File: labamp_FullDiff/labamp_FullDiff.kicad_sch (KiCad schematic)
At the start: 30 parts, among them J1 Conn_02x06_Odd_Even, J2 Conn_02x06_Odd_Even, J3 Conn_01x03, U3 THS4521ID

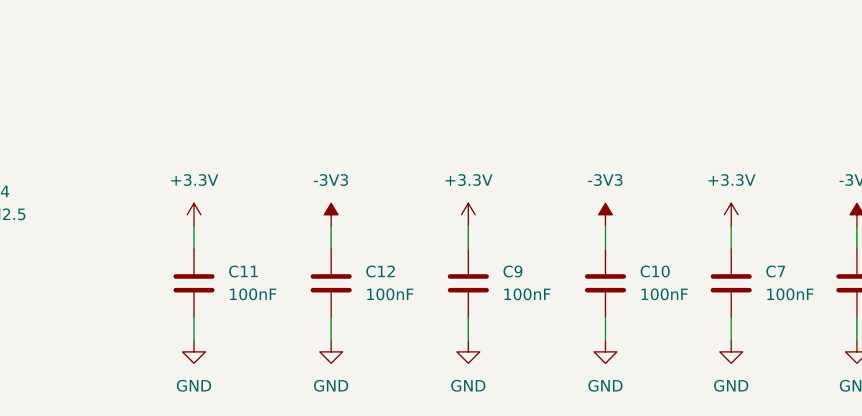
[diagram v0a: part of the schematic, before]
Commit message: PCB layout od Diff ampl started
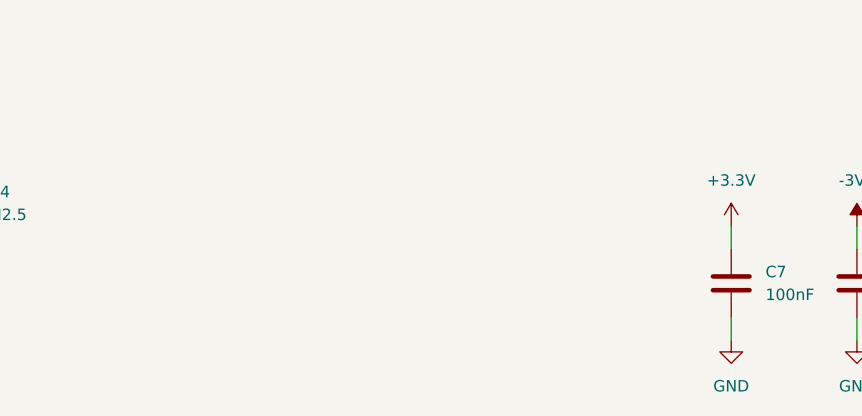
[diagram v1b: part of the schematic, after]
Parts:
- removed C10, C11, C12, C9: 100nF, Capacitor_SMD:C_0603_1608Metric_Pad1.08x0.95mm_HandSolder, symbol Device:C

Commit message: Added option for single supply
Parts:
- added R12, R3: R, Resistor_SMD:R_0603_1608Metric_Pad0.98x0.95mm_HandSolder, symbol Device:R
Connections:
- net +3.3V: now also U3.3 (V_{S+}), R12.2
- net -3V3: now also U3.6 (V_{S-})
- net GND: now also R3.1; no longer U3.2 (V_{OCM})
- new net: R12.1, R3.2, U3.2 (V_{OCM})

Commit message: Updated template PCB layout rules
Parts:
- added C9: 100nF, Capacitor_SMD:C_0603_1608Metric_Pad1.08x0.95mm_HandSolder, symbol Device:C
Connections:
- net GND: now also C9.2
- net at R12.1, R3.2, U3.2 (V_{OCM}): now also C9.1
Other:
- moved on the sheet: R1, R12, R2

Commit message: Added pullup resistors on inputs
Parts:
- added R13, R14: R, Resistor_SMD:R_0603_1608Metric_Pad0.98x0.95mm_HandSolder, symbol Device:R
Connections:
- net +3.3V: now also R13.2, R14.2
- net at R2.2, R5.1, R8.2: now also R14.1
- net at R1.2, R6.1, R9.2: now also R13.1
